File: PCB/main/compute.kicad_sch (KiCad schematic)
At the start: 18 parts, among them J3 UART 3V3 / DNF, J4 PH4 to carrier, SW2 RESET, SW3 BOOT / USER, U1 ESP32-C3-MINI-1-N4

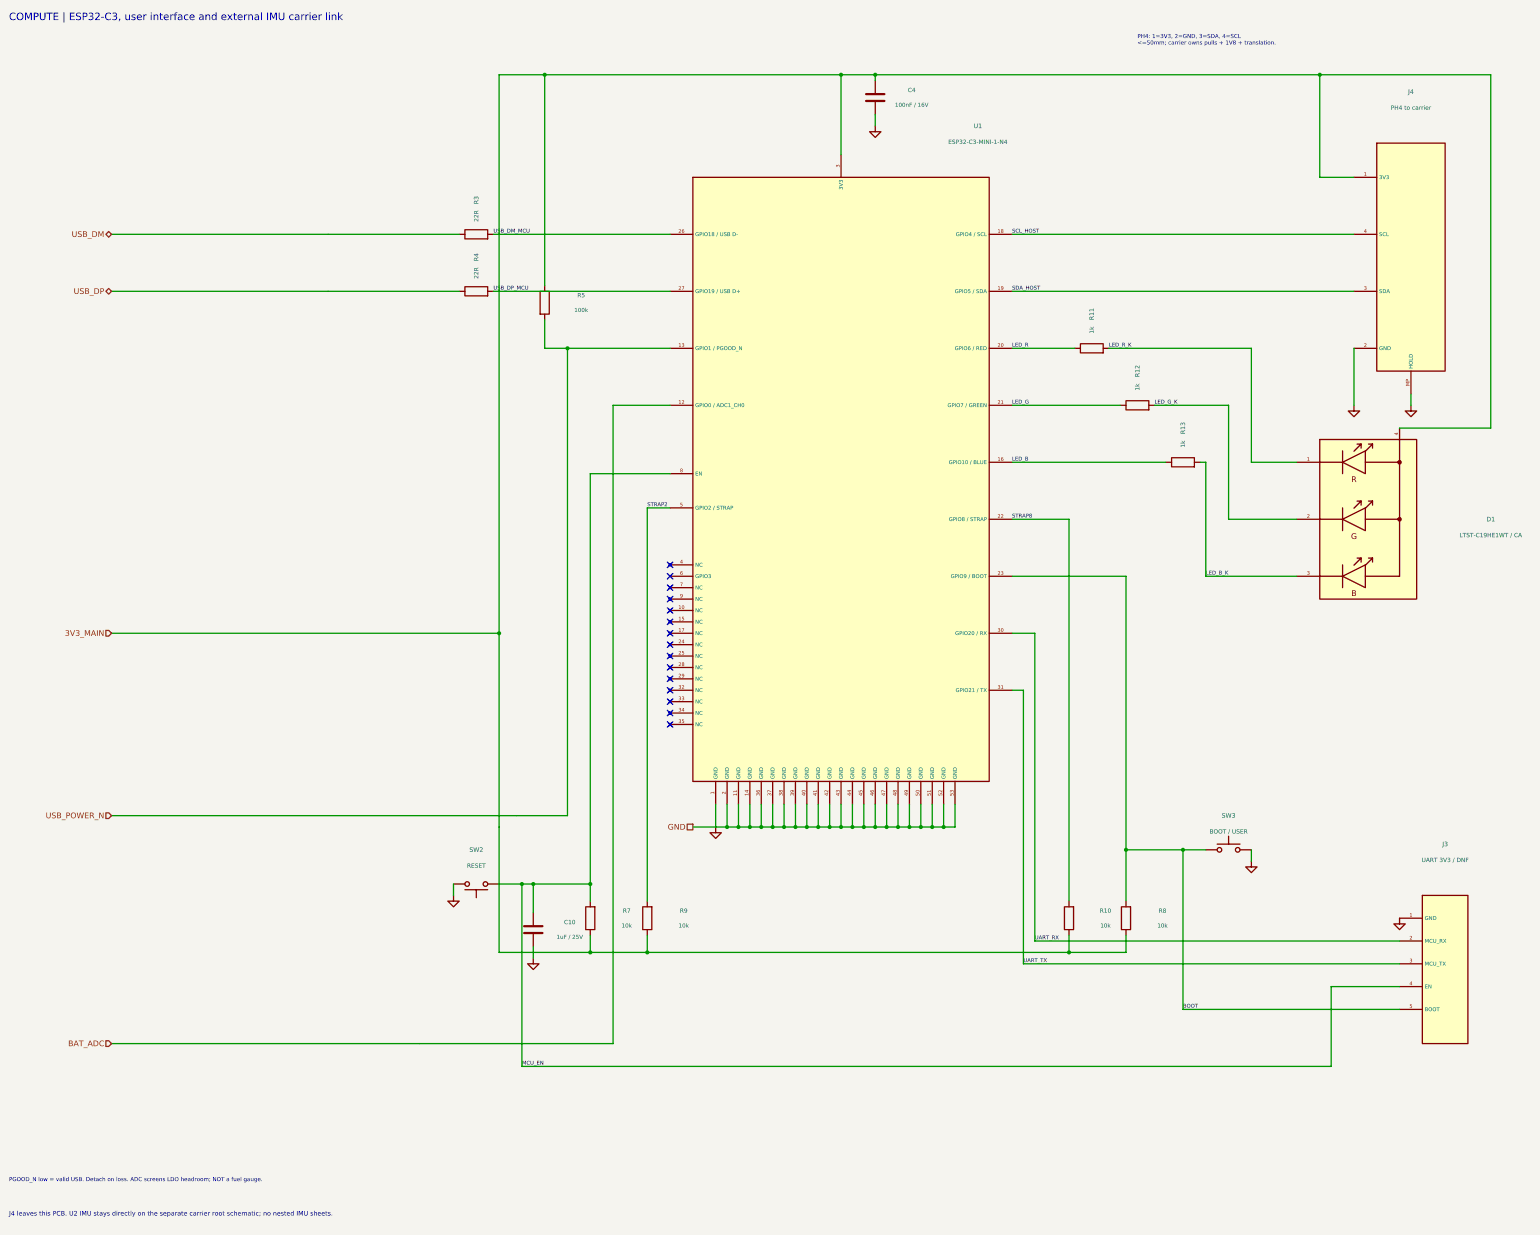
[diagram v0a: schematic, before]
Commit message: Merge compact integrated IMU prototype with diagonal M3 mounting and documented mechanical qualification gates
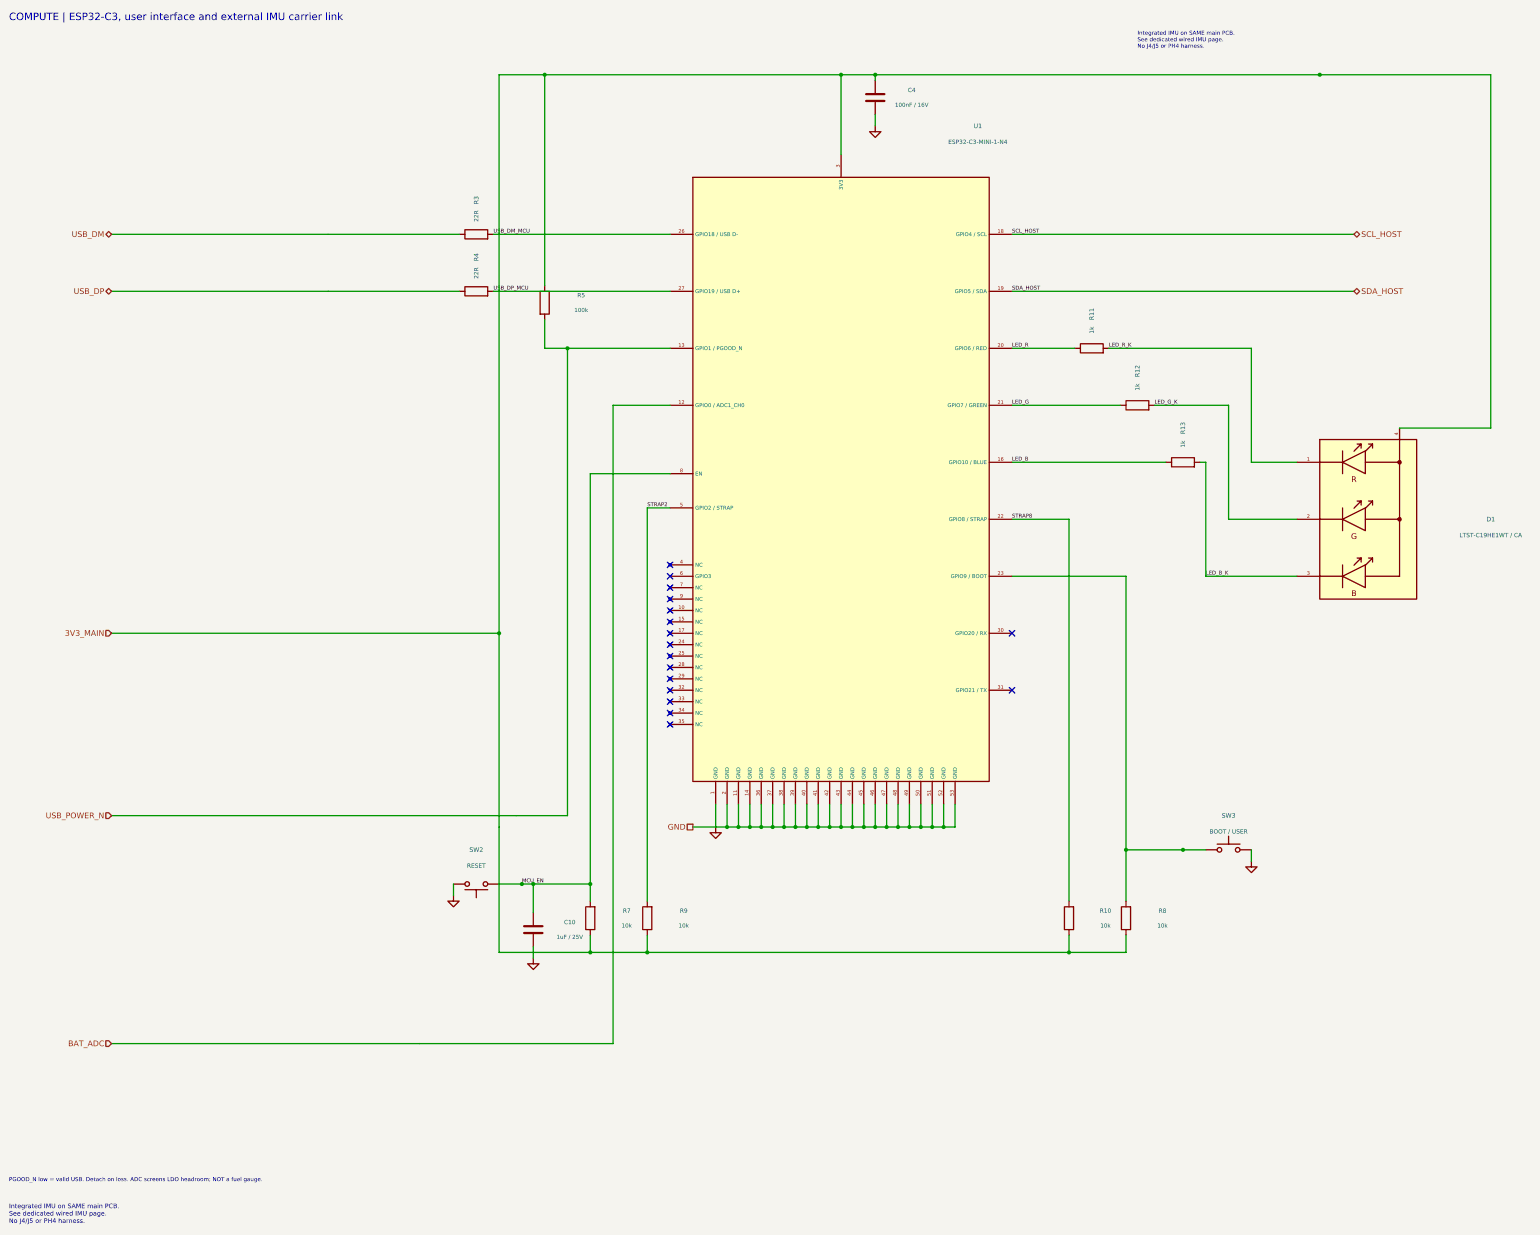
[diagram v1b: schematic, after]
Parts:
- removed J3: UART 3V3 / DNF, smove-r2-main:Debug_5, symbol smove-r2-main:J3
- removed J4: PH4 to carrier, smove-r2-main:JST_PH_S4B-PH-SM4-TB_1x04-1MP_P2.00mm_Horizontal, symbol smove-r2-main:J4
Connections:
- net BOOT: no longer names the net of R8.2, SW3.1, U1.23 (GPIO9 / BOOT)
- net UART_RX: no longer names the net of U1.30 (GPIO20 / RX)
- net UART_TX: no longer names the net of U1.31 (GPIO21 / TX)
- no-connect marks 15 -> 17
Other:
- note added: "Integrated IMU on SAME main PCB. See dedicated wired IMU page. No J4/J5 or PH4 harness."
- note removed: "J4 leaves this PCB. U2 IMU stays directly on the separate carrier root schematic; no nested IMU sheets."
- note removed: "PH4: 1=3V3, 2=GND, 3=SDA, 4=SCL <=50mm; carrier owns pulls + 1V8 + translation."

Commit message: Add better component placements for efficient routing.
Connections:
- net LED_R: now also U1.6 (GPIO3 / RED); no longer U1.20 (GPIO6 / RED)
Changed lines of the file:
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@@
 )
   (no_connect
-    (at 165.1 139.7)
+    (at 241.3 88.9)
 )
   (no_connect
@@
   (wire
     (pts
-      (xy 241.3 88.9)
+      (xy 246.38 88.9)
       (xy 255.27 88.9))
     (stroke
@@
 )
   (label "LED_R"
-    (at 241.3 88.9 0)
+    (at 246.38 88.9 0)
     (effects
       (font
@@
   (no_connect
     (at 241.3 165.1)
+)
+  (label "LED_R"
+    (at 161.29 139.7 0)
+    (effects
+      (font
+        (size .85 .85))
+      (justify left bottom))
+)
+  (wire
+    (pts
+      (xy 161.29 139.7)
+      (xy 165.1 139.7))
+    (stroke
+      (width 0)
+      (type default))
 ))

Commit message: Add Battery on/off switch
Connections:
- net CHG_N: now reaches U1.20 (GPIO6)
- no-connect marks 17 -> 16
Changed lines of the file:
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@@
-)
-  (no_connect
-    (at 241.3 88.9)
 )
   (no_connect
@@
       (width 0)
       (type default))
+)
+  (wire
+    (pts
+      (xy 241.3 88.9)
+      (xy 243.84 88.9))
+    (stroke
+      (width 0)
+      (type default))
+)
+  (wire
+    (pts
+      (xy 243.84 88.9)
+      (xy 243.84 96.52))
+    (stroke
+      (width 0)
+      (type default))
+)
+  (wire
+    (pts
+      (xy 243.84 96.52)
+      (xy 302.26 96.52))
+    (stroke
+      (width 0)
+      (type default))
+)
+  (hierarchical_label "CHG_N"
+    (shape input)
+    (at 302.26 96.52 0)
+    (effects
+      (font
+        (size 1.27 1.27))
+      (justify left))
 ))

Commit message: fab: regenerate JLCPCB assembly/fab outputs for the routed board
- Complete the missing Manufacturer fields (verified against the live LCSC/JLC
  library) on the affected symbols and footprints; no connectivity, geometry,
  routing or value changes.
- Regenerate dist/jlcpcb: bom.csv, pick_and_place.csv, gerber.zip, export-report.json
  from the current board (export.py --overwrite --side top --require-part-numbers).
- BOM: R23 removed, R24/R25 added, TH1 (TDK NTCG103JF103FT1 / C209959) added,
  U4 corrected to XC6220B331MR-G / C86534.
- CPL: R23 row gone; R24, R25 and TH1 rows added.
- DRC: 0 violations, 0 unrouted; one schematic-parity warning (U4 symbol Footprint
  field reads SOT-23-5 while the board uses the identical-land SOT-25_XC6220).
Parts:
- C10, C4: Manufacturer (none) -> Samsung Electro-Mechanics
- D1: Manufacturer (none) -> Lite-On
- R10, R11, R12, R13, R3, R4, R5, R7, R8, R9: Manufacturer (none) -> UNI-ROYAL(Uniroyal Elec)
- SW2, SW3: Manufacturer (none) -> XUNPU
- U1: Manufacturer (none) -> Espressif Systems
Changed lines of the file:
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@@
+          (size 1 1))
+        (hide yes)))
+(property "Manufacturer" "Espressif Systems"
+      (at 203.2 118.11 0)
+      (effects
+        (font
           (size 1 1))
         (hide yes)))
@@
           (size 1 1))
         (hide yes)))
+(property "Manufacturer" "XUNPU"
+      (at 121.92 208.28 0)
+      (effects
+        (font
+          (size 1 1))
+        (hide yes)))
     (pin "1"
 )
@@
           (size 1 1))
         (hide yes)))
+(property "Manufacturer" "XUNPU"
+      (at 289.56 200.66 0)
+      (effects
+        (font
+          (size 1 1))
+        (hide yes)))
     (pin "1"
 )
@@
           (size 1 1))
         (hide yes)))
+(property "Manufacturer" "Lite-On"
+      (at 322.58 127 0)
+      (effects
+        (font
+          (size 1 1))
+        (hide yes)))
     (pin "1"
 )
@@
           (size 1 1))
         (hide yes)))
+(property "Manufacturer" "UNI-ROYAL(Uniroyal Elec)"
+      (at 121.92 63.5 0)
+      (effects
+        (font
+          (size 1 1))
+        (hide yes)))
     (pin "1"
 )
@@
           (size 1 1))
         (hide yes)))
+(property "Manufacturer" "UNI-ROYAL(Uniroyal Elec)"
+      (at 121.92 76.2 0)
+      (effects
+        (font
+          (size 1 1))
+        (hide yes)))
     (pin "1"
 )
@@
           (size 1 1))
         (hide yes)))
+(property "Manufacturer" "UNI-ROYAL(Uniroyal Elec)"
+      (at 137.16 78.74 0)
+      (effects
+        (font
+          (size 1 1))
+        (hide yes)))
     (pin "1"
 )
@@
           (size 1 1))
         (hide yes)))
+(property "Manufacturer" "UNI-ROYAL(Uniroyal Elec)"
+      (at 147.32 215.9 0)
+      (effects
+        (font
+          (size 1 1))
+        (hide yes)))
     (pin "1"
 )
@@
           (size 1 1))
         (hide yes)))
+(property "Manufacturer" "UNI-ROYAL(Uniroyal Elec)"
+      (at 266.7 215.9 0)
+      (effects
+        (font
+          (size 1 1))
+        (hide yes)))
     (pin "1"
 )
@@
           (size 1 1))
         (hide yes)))
+(property "Manufacturer" "UNI-ROYAL(Uniroyal Elec)"
+      (at 160.02 215.9 0)
+      (effects
+        (font
+          (size 1 1))
+        (hide yes)))
     (pin "1"
 )
@@
         (hide yes)))
     (property "LCSC" "C25744"
+      (at 254 215.9 0)
+      (effects
+        (font
+          (size 1 1))
+        (hide yes)))
+(property "Manufacturer" "UNI-ROYAL(Uniroyal Elec)"
       (at 254 215.9 0)
       (effects
@@
           (size 1 1))
         (hide yes)))
+(property "Manufacturer" "UNI-ROYAL(Uniroyal Elec)"
+      (at 259.08 88.9 0)
+      (effects
+        (font
+          (size 1 1))
+        (hide yes)))
     (pin "1"
 )
@@
           (size 1 1))
         (hide yes)))
+(property "Manufacturer" "UNI-ROYAL(Uniroyal Elec)"
+      (at 269.24 101.6 0)
+      (effects
+        (font
+          (size 1 1))
+        (hide yes)))
     (pin "1"
 )
@@
           (size 1 1))
         (hide yes)))
+(property "Manufacturer" "UNI-ROYAL(Uniroyal Elec)"
+      (at 279.4 114.3 0)
+      (effects
+        (font
+          (size 1 1))
+        (hide yes)))
     (pin "1"
 )
@@
           (size 1 1))
         (hide yes)))
+(property "Manufacturer" "Samsung Electro-Mechanics"
+      (at 210.82 33.02 0)
+      (effects
+        (font
+          (size 1 1))
+        (hide yes)))
     (pin "1"
 )
@@
       (at 134.62 218.44 0)
       (effects
+        (font
+          (size 1 1))
+        (hide yes)))
+(property "Manufacturer" "Samsung Electro-Mechanics"
+      (at 134.62 218.44 0)
+      (effects
